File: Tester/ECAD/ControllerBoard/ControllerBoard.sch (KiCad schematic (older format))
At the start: 0 parts

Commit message: Progressed motor control PCB.
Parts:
- added J? (x4): Conn_01x02_Male, symbol Connector:Conn_01x02_Male
- added J?: Barrel_Jack, symbol Connector:Barrel_Jack
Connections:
- net labels added: +12V, GND
- wire segments 0 -> 24
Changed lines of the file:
@@
 $EndDescr
 $Sheet
-S 5100 1000 1450 5650
+S 5950 1250 2050 4650
 U 5E5070AC
 F0 "MCU" 50
 F1 "MCU.sch" 50
+F2 "MOTOR_CTRL_1A" O R 8000 1550 50
+F3 "MOTOR_CTRL_1B" O R 8000 1650 50
+F4 "MOTOR_CTRL_2A" O R 8000 1800 50
+F5 "MOTOR_CTRL_2B" O R 8000 1900 50
+F6 "MOTOR_CTRL_3A" O R 8000 2050 50
+F7 "MOTOR_CTRL_3B" O R 8000 2150 50
+F8 "MOTOR_CTRL_4A" O R 8000 2300 50
+F9 "MOTOR_CTRL_4B" O R 8000 2400 50
+F10 "MOTOR_FAULT_12" I R 8000 2550 50
+F11 "MOTOR_FAULT_34" I R 8000 2650 50
+F12 "MOTOR_SLEEP_12" O R 8000 2800 50
+F13 "MOTOR_SLEPP_34" O R 8000 2900 50
 $EndSheet
 $Sheet
-S 7200 1050 1200 950
+S 8650 1250 1350 2100
 U 5E507163
 F0 "Motor Control" 50
 F1 "MotorControl.sch" 50
+F2 "12V_POWER_IN" I L 8650 1350 50
+F3 "GND" I L 8650 3250 50
+F4 "MOTOR_OUT_2-" O R 10000 1700 50
+F5 "MOTOR_OUT_2+" O R 10000 1600 50
+F6 "MOTOR_OUT_1-" O R 10000 1450 50
+F7 "MOTOR_OUT_1+" O R 10000 1350 50
+F8 "MOTOR_OUT_4-" O R 10000 2200 50
+F9 "MOTOR_OUT_4+" O R 10000 2100 50
+F10 "MOTOR_OUT_3-" O R 10000 1950 50
+F11 "MOTOR_OUT_3+" O R 10000 1850 50
+F12 "MOTOR_CTRL_1A" I L 8650 1550 50
+F13 "MOTOR_CTRL_1B" I L 8650 1650 50
+F14 "MOTOR_CTRL_2A" I L 8650 1800 50
+F15 "MOTOR_CTRL_2B" I L 8650 1900 50
+F16 "MOTOR_CTRL_3A" I L 8650 2050 50
+F17 "MOTOR_CTRL_3B" I L 8650 2150 50
+F18 "MOTOR_CTRL_4A" I L 8650 2300 50
+F19 "MOTOR_CTRL_4B" I L 8650 2400 50
+F20 "MOTOR_FAULT_12" O L 8650 2550 50
+F21 "MOTOR_FAULT_34" O L 8650 2650 50
+F22 "MOTOR_SLEEP_12" I L 8650 2800 50
+F23 "MOTOR_SLEEP_34" I L 8650 2900 50
 $EndSheet
 $Sheet
-S 3000 1000 1400 5650
+S 3000 1250 1400 5650
 U 5E55806E
 F0 "Signal I/O" 50
 F1 "SignalInputOuput.sch" 50
 $EndSheet
+$Comp
+L Connector:Conn_01x02_Male J?
+U 1 1 5E51F506
+P 10200 1450
+AR Path="/5E507163/5E51F506" Ref="J?"  Part="1"
+AR Path="/5E51F506" Ref="J?"  Part="1"
+F 0 "J?" H 10172 1332 50  0000 R CNN
+F 1 "Conn_01x02_Male" H 10172 1423 50  0000 R CNN
+F 2 "" H 10200 1450 50  0001 C CNN
+F 3 "~" H 10200 1450 50  0001 C CNN
+	1    10200 1450
+	-1   0    0    1
+$EndComp
+$Comp
+L Connector:Conn_01x02_Male J?
+U 1 1 5E51F50C
+P 10200 1700
+AR Path="/5E507163/5E51F50C" Ref="J?"  Part="1"
+AR Path="/5E51F50C" Ref="J?"  Part="1"
+F 0 "J?" H 10172 1582 50  0000 R CNN
+F 1 "Conn_01x02_Male" H 10172 1673 50  0000 R CNN
+F 2 "" H 10200 1700 50  0001 C CNN
+F 3 "~" H 10200 1700 50  0001 C CNN
+	1    10200 1700
+	-1   0    0    1
+$EndComp
+$Comp
+L Connector:Conn_01x02_Male J?
+U 1 1 5E51F512
+P 10200 1950
+AR Path="/5E507163/5E51F512" Ref="J?"  Part="1"
+AR Path="/5E51F512" Ref="J?"  Part="1"
+F 0 "J?" H 10172 1832 50  0000 R CNN
+F 1 "Conn_01x02_Male" H 10172 1923 50  0000 R CNN
+F 2 "" H 10200 1950 50  0001 C CNN
+F 3 "~" H 10200 1950 50  0001 C CNN
+	1    10200 1950
+	-1   0    0    1
+$EndComp
+$Comp
+L Connector:Conn_01x02_Male J?
+U 1 1 5E51F518
+P 10200 2200
+AR Path="/5E507163/5E51F518" Ref="J?"  Part="1"
+AR Path="/5E51F518" Ref="J?"  Part="1"
+F 0 "J?" H 10172 2082 50  0000 R CNN
+F 1 "Conn_01x02_Male" H 10172 2173 50  0000 R CNN
+F 2 "" H 10200 2200 50  0001 C CNN
+F 3 "~" H 10200 2200 50  0001 C CNN
+	1    10200 2200
+	-1   0    0    1
+$EndComp
+$Comp
+L Connector:Barrel_Jack J?
+U 1 1 5E526230
+P 1050 1050
+F 0 "J?" H 1107 1375 50  0000 C CNN
+F 1 "Barrel_Jack" H 1107 1284 50  0000 C CNN
+F 2 "" H 1100 1010 50  0001 C CNN
+F 3 "~" H 1100 1010 50  0001 C CNN
+	1    1050 1050
+	1    0    0    -1
+$EndComp
+Wire Wire Line
+	1350 950  2050 950
+Wire Wire Line
+	6800 7550 4800 7550
+Wire Wire Line
+	1500 7550 1500 1150
+Wire Wire Line
+	1500 1150 1350 1150
+$Comp
+L power:GND #PWR?
+U 1 1 5E52861B
+P 4800 7550
+F 0 "#PWR?" H 4800 7300 50  0001 C CNN
+F 1 "GND" H 4805 7377 50  0000 C CNN
+F 2 "" H 4800 7550 50  0001 C CNN
+F 3 "" H 4800 7550 50  0001 C CNN
+	1    4800 7550
+	1    0    0    -1
+$EndComp
+Connection ~ 4800 7550
+Wire Wire Line
+	4800 7550 1500 7550
+$Comp
+L power:+12V #PWR?
+U 1 1 5E52879A
+P 2050 950
+F 0 "#PWR?" H 2050 800 50  0001 C CNN
+F 1 "+12V" H 2065 1123 50  0000 C CNN
+F 2 "" H 2050 950 50  0001 C CNN
+F 3 "" H 2050 950 50  0001 C CNN
+	1    2050 950
+	1    0    0    -1
+$EndComp
+Connection ~ 2050 950
+Wire Wire Line
+	6800 7550 6800 6300
+Wire Wire Line
+	8650 3250 8450 3250
+Wire Wire Line
+	8450 3250 8450 6300
+Wire Wire Line
+	6800 6300 8450 6300
+Wire Wire Line
+	8650 1350 8450 1350
+Wire Wire Line
+	8450 1350 8450 950
+Wire Wire Line
+	2050 950  8450 950
+Wire Wire Line
+	8000 1550 8650 1550
+Wire Wire Line
+	8650 1650 8000 1650
+Wire Wire Line
+	8000 1800 8650 1800
+Wire Wire Line
+	8650 1900 8000 1900
+Wire Wire Line
+	8000 2050 8650 2050
+Wire Wire Line
+	8650 2150 8000 2150
+Wire Wire Line
+	8000 2300 8650 2300
+Wire Wire Line
+	8650 2400 8000 2400
+Wire Wire Line
+	8000 2550 8650 2550
+Wire Wire Line
+	8650 2650 8000 2650
+Wire Wire Line
+	8000 2800 8650 2800
+Wire Wire Line
+	8650 2900 8000 2900
 $EndSCHEMATC

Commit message: Added the Manufacturer Part Number component field.
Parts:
- J? (x5): Manufacturer Part Number (none) -> tbd
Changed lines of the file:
@@
 F 2 "" H 10200 1450 50  0001 C CNN
 F 3 "~" H 10200 1450 50  0001 C CNN
+F 4 "tbd" H 10200 1450 50  0001 C CNN "Manufacturer Part Number"
 	1    10200 1450
 	-1   0    0    1
@@
 F 2 "" H 10200 1700 50  0001 C CNN
 F 3 "~" H 10200 1700 50  0001 C CNN
+F 4 "tbd" H 10200 1700 50  0001 C CNN "Manufacturer Part Number"
 	1    10200 1700
 	-1   0    0    1
@@
 F 2 "" H 10200 1950 50  0001 C CNN
 F 3 "~" H 10200 1950 50  0001 C CNN
+F 4 "tbd" H 10200 1950 50  0001 C CNN "Manufacturer Part Number"
 	1    10200 1950
 	-1   0    0    1
@@
 F 2 "" H 10200 2200 50  0001 C CNN
 F 3 "~" H 10200 2200 50  0001 C CNN
+F 4 "tbd" H 10200 2200 50  0001 C CNN "Manufacturer Part Number"
 	1    10200 2200
 	-1   0    0    1
@@
 F 2 "" H 1100 1010 50  0001 C CNN
 F 3 "~" H 1100 1010 50  0001 C CNN
+F 4 "tbd" H 1050 1050 50  0001 C CNN "Manufacturer Part Number"
 	1    1050 1050
 	1    0    0    -1

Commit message: Progressed component assignment.
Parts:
- J?: Manufacturer Part Number tbd -> PJ-037B
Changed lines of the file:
@@
 F 1 "Barrel_Jack" H 1107 1284 50  0000 C CNN
 F 2 "" H 1100 1010 50  0001 C CNN
-F 3 "~" H 1100 1010 50  0001 C CNN
-F 4 "tbd" H 1050 1050 50  0001 C CNN "Manufacturer Part Number"
+F 3 "https://www.cuidevices.com/product/resource/pj-037b.pdf" H 1100 1010 50  0001 C CNN
+F 4 "PJ-037B" H 1050 1050 50  0001 C CNN "Manufacturer Part Number"
 	1    1050 1050
 	1    0    0    -1

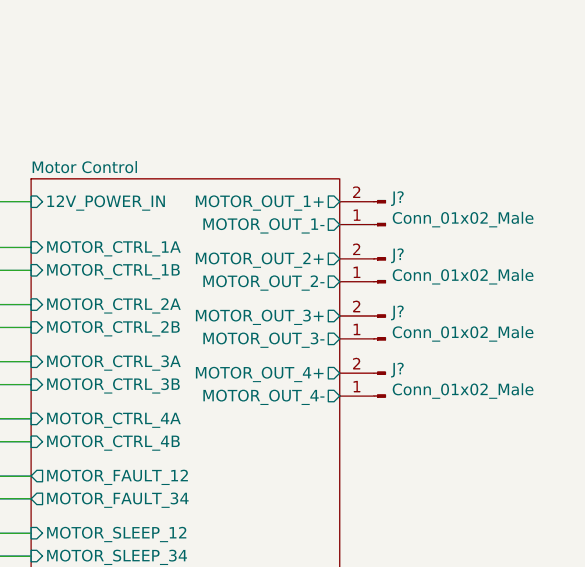
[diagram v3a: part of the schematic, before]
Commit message: Progressed component assigment.
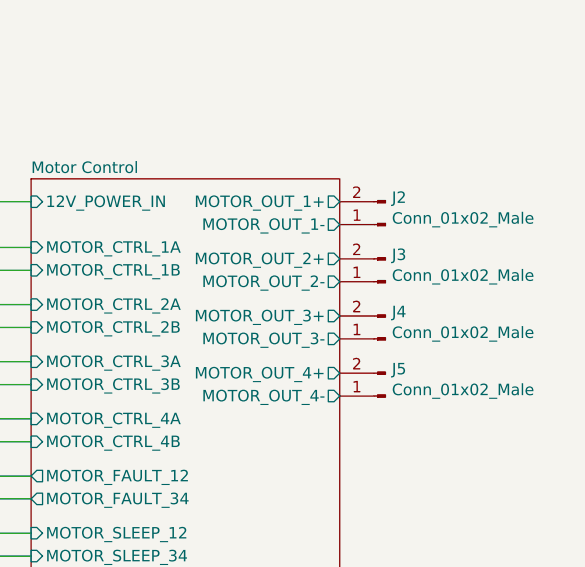
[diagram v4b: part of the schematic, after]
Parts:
- J2, J3, J4, J5: renamed from J?; Manufacturer Part Number tbd -> 0530480210
- gave numbers to parts that had none: 1
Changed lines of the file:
@@
 P 10200 1450
 AR Path="/5E507163/5E51F506" Ref="J?"  Part="1"
-AR Path="/5E51F506" Ref="J?"  Part="1"
-F 0 "J?" H 10172 1332 50  0000 R CNN
+AR Path="/5E51F506" Ref="J2"  Part="1"
+F 0 "J2" H 10172 1332 50  0000 R CNN
 F 1 "Conn_01x02_Male" H 10172 1423 50  0000 R CNN
 F 2 "" H 10200 1450 50  0001 C CNN
 F 3 "~" H 10200 1450 50  0001 C CNN
-F 4 "tbd" H 10200 1450 50  0001 C CNN "Manufacturer Part Number"
+F 4 "0530480210" H 10200 1450 50  0001 C CNN "Manufacturer Part Number"
 	1    10200 1450
 	-1   0    0    1
@@
 P 10200 1700
 AR Path="/5E507163/5E51F50C" Ref="J?"  Part="1"
-AR Path="/5E51F50C" Ref="J?"  Part="1"
-F 0 "J?" H 10172 1582 50  0000 R CNN
+AR Path="/5E51F50C" Ref="J3"  Part="1"
+F 0 "J3" H 10172 1582 50  0000 R CNN
 F 1 "Conn_01x02_Male" H 10172 1673 50  0000 R CNN
 F 2 "" H 10200 1700 50  0001 C CNN
 F 3 "~" H 10200 1700 50  0001 C CNN
-F 4 "tbd" H 10200 1700 50  0001 C CNN "Manufacturer Part Number"
+F 4 "0530480210" H 10200 1700 50  0001 C CNN "Manufacturer Part Number"
 	1    10200 1700
 	-1   0    0    1
@@
 P 10200 1950
 AR Path="/5E507163/5E51F512" Ref="J?"  Part="1"
-AR Path="/5E51F512" Ref="J?"  Part="1"
-F 0 "J?" H 10172 1832 50  0000 R CNN
+AR Path="/5E51F512" Ref="J4"  Part="1"
+F 0 "J4" H 10172 1832 50  0000 R CNN
 F 1 "Conn_01x02_Male" H 10172 1923 50  0000 R CNN
 F 2 "" H 10200 1950 50  0001 C CNN
 F 3 "~" H 10200 1950 50  0001 C CNN
-F 4 "tbd" H 10200 1950 50  0001 C CNN "Manufacturer Part Number"
+F 4 "0530480210" H 10200 1950 50  0001 C CNN "Manufacturer Part Number"
 	1    10200 1950
 	-1   0    0    1
@@
 P 10200 2200
 AR Path="/5E507163/5E51F518" Ref="J?"  Part="1"
-AR Path="/5E51F518" Ref="J?"  Part="1"
-F 0 "J?" H 10172 2082 50  0000 R CNN
+AR Path="/5E51F518" Ref="J5"  Part="1"
+F 0 "J5" H 10172 2082 50  0000 R CNN
 F 1 "Conn_01x02_Male" H 10172 2173 50  0000 R CNN
 F 2 "" H 10200 2200 50  0001 C CNN
 F 3 "~" H 10200 2200 50  0001 C CNN
-F 4 "tbd" H 10200 2200 50  0001 C CNN "Manufacturer Part Number"
+F 4 "0530480210" H 10200 2200 50  0001 C CNN "Manufacturer Part Number"
 	1    10200 2200
 	-1   0    0    1
 $EndComp
 $Comp
-L Connector:Barrel_Jack J?
+L Connector:Barrel_Jack J1
 U 1 1 5E526230
 P 1050 1050
-F 0 "J?" H 1107 1375 50  0000 C CNN
+F 0 "J1" H 1107 1375 50  0000 C CNN
 F 1 "Barrel_Jack" H 1107 1284 50  0000 C CNN
 F 2 "" H 1100 1010 50  0001 C CNN
@@
 	1500 1150 1350 1150
 $Comp
-L power:GND #PWR?
+L power:GND #PWR02
 U 1 1 5E52861B
 P 4800 7550
-F 0 "#PWR?" H 4800 7300 50  0001 C CNN
+F 0 "#PWR02" H 4800 7300 50  0001 C CNN
 F 1 "GND" H 4805 7377 50  0000 C CNN
 F 2 "" H 4800 7550 50  0001 C CNN
@@
 	4800 7550 1500 7550
 $Comp
-L power:+12V #PWR?
+L power:+12V #PWR01
 U 1 1 5E52879A
 P 2050 950
-F 0 "#PWR?" H 2050 800 50  0001 C CNN
+F 0 "#PWR01" H 2050 800 50  0001 C CNN
 F 1 "+12V" H 2065 1123 50  0000 C CNN
 F 2 "" H 2050 950 50  0001 C CNN

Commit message: Component assigment cont.
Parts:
- J2, J3, J4, J5: footprint (none) -> Connector_Molex:Molex_PicoBlade_53048-0210_1x02_P1.25mm_Horizontal
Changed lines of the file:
@@
 F 0 "J2" H 10172 1332 50  0000 R CNN
 F 1 "Conn_01x02_Male" H 10172 1423 50  0000 R CNN
-F 2 "" H 10200 1450 50  0001 C CNN
+F 2 "Connector_Molex:Molex_PicoBlade_53048-0210_1x02_P1.25mm_Horizontal" H 10200 1450 50  0001 C CNN
 F 3 "~" H 10200 1450 50  0001 C CNN
 F 4 "0530480210" H 10200 1450 50  0001 C CNN "Manufacturer Part Number"
@@
 F 0 "J3" H 10172 1582 50  0000 R CNN
 F 1 "Conn_01x02_Male" H 10172 1673 50  0000 R CNN
-F 2 "" H 10200 1700 50  0001 C CNN
+F 2 "Connector_Molex:Molex_PicoBlade_53048-0210_1x02_P1.25mm_Horizontal" H 10200 1700 50  0001 C CNN
 F 3 "~" H 10200 1700 50  0001 C CNN
 F 4 "0530480210" H 10200 1700 50  0001 C CNN "Manufacturer Part Number"
@@
 F 0 "J4" H 10172 1832 50  0000 R CNN
 F 1 "Conn_01x02_Male" H 10172 1923 50  0000 R CNN
-F 2 "" H 10200 1950 50  0001 C CNN
+F 2 "Connector_Molex:Molex_PicoBlade_53048-0210_1x02_P1.25mm_Horizontal" H 10200 1950 50  0001 C CNN
 F 3 "~" H 10200 1950 50  0001 C CNN
 F 4 "0530480210" H 10200 1950 50  0001 C CNN "Manufacturer Part Number"
@@
 F 0 "J5" H 10172 2082 50  0000 R CNN
 F 1 "Conn_01x02_Male" H 10172 2173 50  0000 R CNN
-F 2 "" H 10200 2200 50  0001 C CNN
+F 2 "Connector_Molex:Molex_PicoBlade_53048-0210_1x02_P1.25mm_Horizontal" H 10200 2200 50  0001 C CNN
 F 3 "~" H 10200 2200 50  0001 C CNN
 F 4 "0530480210" H 10200 2200 50  0001 C CNN "Manufacturer Part Number"

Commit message: Progressed control board schematic.
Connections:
- wire segments 24 -> 39
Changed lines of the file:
@@
 $Descr A4 11693 8268
 encoding utf-8
-Sheet 1 4
+Sheet 1 5
 Title ""
 Date ""
@@
 F11 "MOTOR_FAULT_34" I R 8000 2650 50
 F12 "MOTOR_SLEEP_12" O R 8000 2800 50
-F13 "MOTOR_SLEPP_34" O R 8000 2900 50
+F13 "MOTOR_SLEEP_34" O R 8000 2900 50
+F14 "GND" I L 5950 5800 50
+F15 "VMCU" I L 5950 1400 50
 $EndSheet
 $Sheet
@@
 F0 "Motor Control" 50
 F1 "MotorControl.sch" 50
-F2 "12V_POWER_IN" I L 8650 1350 50
-F3 "GND" I L 8650 3250 50
-F4 "MOTOR_OUT_2-" O R 10000 1700 50
-F5 "MOTOR_OUT_2+" O R 10000 1600 50
-F6 "MOTOR_OUT_1-" O R 10000 1450 50
-F7 "MOTOR_OUT_1+" O R 10000 1350 50
-F8 "MOTOR_OUT_4-" O R 10000 2200 50
-F9 "MOTOR_OUT_4+" O R 10000 2100 50
-F10 "MOTOR_OUT_3-" O R 10000 1950 50
-F11 "MOTOR_OUT_3+" O R 10000 1850 50
-F12 "MOTOR_CTRL_1A" I L 8650 1550 50
-F13 "MOTOR_CTRL_1B" I L 8650 1650 50
-F14 "MOTOR_CTRL_2A" I L 8650 1800 50
-F15 "MOTOR_CTRL_2B" I L 8650 1900 50
-F16 "MOTOR_CTRL_3A" I L 8650 2050 50
-F17 "MOTOR_CTRL_3B" I L 8650 2150 50
-F18 "MOTOR_CTRL_4A" I L 8650 2300 50
-F19 "MOTOR_CTRL_4B" I L 8650 2400 50
-F20 "MOTOR_FAULT_12" O L 8650 2550 50
-F21 "MOTOR_FAULT_34" O L 8650 2650 50
-F22 "MOTOR_SLEEP_12" I L 8650 2800 50
-F23 "MOTOR_SLEEP_34" I L 8650 2900 50
-$EndSheet
-$Sheet
-S 3000 1250 1400 5650
+F2 "GND" I L 8650 3250 50
+F3 "MOTOR_OUT_2-" O R 10000 1700 50
+F4 "MOTOR_OUT_2+" O R 10000 1600 50
+F5 "MOTOR_OUT_1-" O R 10000 1450 50
+F6 "MOTOR_OUT_1+" O R 10000 1350 50
+F7 "MOTOR_OUT_4-" O R 10000 2200 50
+F8 "MOTOR_OUT_4+" O R 10000 2100 50
+F9 "MOTOR_OUT_3-" O R 10000 1950 50
+F10 "MOTOR_OUT_3+" O R 10000 1850 50
+F11 "MOTOR_CTRL_1A" I L 8650 1550 50
+F12 "MOTOR_CTRL_1B" I L 8650 1650 50
+F13 "MOTOR_CTRL_2A" I L 8650 1800 50
+F14 "MOTOR_CTRL_2B" I L 8650 1900 50
+F15 "MOTOR_CTRL_3A" I L 8650 2050 50
+F16 "MOTOR_CTRL_3B" I L 8650 2150 50
+F17 "MOTOR_CTRL_4A" I L 8650 2300 50
+F18 "MOTOR_CTRL_4B" I L 8650 2400 50
+F19 "MOTOR_FAULT_12" O L 8650 2550 50
+F20 "MOTOR_FAULT_34" O L 8650 2650 50
+F21 "MOTOR_SLEEP_12" I L 8650 2800 50
+F22 "MOTOR_SLEEP_34" I L 8650 2900 50
+F23 "VMOTOR" I L 8650 1350 50
+$EndSheet
+$Sheet
+S 4100 1250 1400 5650
 U 5E55806E
 F0 "Signal I/O" 50
@@
 $EndComp
 Wire Wire Line
-	1350 950  2050 950
-Wire Wire Line
-	6800 7550 4800 7550
-Wire Wire Line
-	1500 7550 1500 1150
+	6800 7550 5750 7550
 Wire Wire Line
 	1500 1150 1350 1150
@@
 L power:+12V #PWR01
 U 1 1 5E52879A
-P 2050 950
-F 0 "#PWR01" H 2050 800 50  0001 C CNN
-F 1 "+12V" H 2065 1123 50  0000 C CNN
-F 2 "" H 2050 950 50  0001 C CNN
-F 3 "" H 2050 950 50  0001 C CNN
-	1    2050 950
+P 1550 950
+F 0 "#PWR01" H 1550 800 50  0001 C CNN
+F 1 "+12V" H 1565 1123 50  0000 C CNN
+F 2 "" H 1550 950 50  0001 C CNN
+F 3 "" H 1550 950 50  0001 C CNN
+	1    1550 950
 	1    0    0    -1
 $EndComp
-Connection ~ 2050 950
 Wire Wire Line
 	6800 7550 6800 6300
@@
 	6800 6300 8450 6300
 Wire Wire Line
-	8650 1350 8450 1350
-Wire Wire Line
-	8450 1350 8450 950
-Wire Wire Line
-	2050 950  8450 950
-Wire Wire Line
 	8000 1550 8650 1550
 Wire Wire Line
@@
 Wire Wire Line
 	8650 2900 8000 2900
+Wire Wire Line
+	5950 5800 5750 5800
+Wire Wire Line
+	5750 5800 5750 7550
+Connection ~ 5750 7550
+Wire Wire Line
+	5750 7550 4800 7550
+$Sheet
+S 1900 1250 1550 1700
+U 5E55CCDC
+F0 "Power" 50
+F1 "Power.sch" 50
+F2 "12V_POWER_IN" I L 1900 1350 50
+F3 "GND" I L 1900 2850 50
+F4 "VMOTOR" O R 3450 1350 50
+F5 "VMCU" O R 3450 1500 50
+$EndSheet
+Wire Wire Line
+	1700 950  1550 950
+Connection ~ 1550 950
+Wire Wire Line
+	1550 950  1350 950
+Wire Wire Line
+	1500 1150 1500 2850
+Wire Wire Line
+	1900 1350 1700 1350
+Wire Wire Line
+	1700 1350 1700 950
+Wire Wire Line
+	1900 2850 1500 2850
+Connection ~ 1500 2850
+Wire Wire Line
+	1500 2850 1500 7550
+Wire Wire Line
+	3450 1350 3650 1350
+Wire Wire Line
+	3650 1350 3650 650
+Wire Wire Line
+	3650 650  8400 650
+Wire Wire Line
+	8400 650  8400 1350
+Wire Wire Line
+	8400 1350 8650 1350
+Wire Wire Line
+	3450 1500 3850 1500
+Wire Wire Line
+	3850 1500 3850 800
+Wire Wire Line
+	3850 800  5700 800
+Wire Wire Line
+	5950 1400 5700 1400
+Wire Wire Line
+	5700 1400 5700 800
 $EndSCHEMATC

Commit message: Progressed circuit layout.
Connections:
- wire segments 39 -> 59
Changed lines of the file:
@@
 $EndDescr
-$Sheet
-S 5950 1250 2050 4650
-U 5E5070AC
-F0 "MCU" 50
-F1 "MCU.sch" 50
-F2 "MOTOR_CTRL_1A" O R 8000 1550 50
-F3 "MOTOR_CTRL_1B" O R 8000 1650 50
-F4 "MOTOR_CTRL_2A" O R 8000 1800 50
-F5 "MOTOR_CTRL_2B" O R 8000 1900 50
-F6 "MOTOR_CTRL_3A" O R 8000 2050 50
-F7 "MOTOR_CTRL_3B" O R 8000 2150 50
-F8 "MOTOR_CTRL_4A" O R 8000 2300 50
-F9 "MOTOR_CTRL_4B" O R 8000 2400 50
-F10 "MOTOR_FAULT_12" I R 8000 2550 50
-F11 "MOTOR_FAULT_34" I R 8000 2650 50
-F12 "MOTOR_SLEEP_12" O R 8000 2800 50
-F13 "MOTOR_SLEEP_34" O R 8000 2900 50
-F14 "GND" I L 5950 5800 50
-F15 "VMCU" I L 5950 1400 50
-$EndSheet
 $Sheet
 S 8650 1250 1350 2100
@@
 F23 "VMOTOR" I L 8650 1350 50
 $EndSheet
-$Sheet
-S 4100 1250 1400 5650
-U 5E55806E
-F0 "Signal I/O" 50
-F1 "SignalInputOuput.sch" 50
-$EndSheet
 $Comp
 L Connector:Conn_01x02_Male J?
@@
 L power:GND #PWR02
 U 1 1 5E52861B
-P 4800 7550
-F 0 "#PWR02" H 4800 7300 50  0001 C CNN
-F 1 "GND" H 4805 7377 50  0000 C CNN
-F 2 "" H 4800 7550 50  0001 C CNN
-F 3 "" H 4800 7550 50  0001 C CNN
-	1    4800 7550
+P 4600 7550
+F 0 "#PWR02" H 4600 7300 50  0001 C CNN
+F 1 "GND" H 4605 7377 50  0000 C CNN
+F 2 "" H 4600 7550 50  0001 C CNN
+F 3 "" H 4600 7550 50  0001 C CNN
+	1    4600 7550
 	1    0    0    -1
 $EndComp
-Connection ~ 4800 7550
-Wire Wire Line
-	4800 7550 1500 7550
 $Comp
 L power:+12V #PWR01
@@
 Wire Wire Line
 	5750 5800 5750 7550
-Connection ~ 5750 7550
-Wire Wire Line
-	5750 7550 4800 7550
+Wire Wire Line
+	1700 950  1550 950
+Connection ~ 1550 950
+Wire Wire Line
+	1550 950  1350 950
+Wire Wire Line
+	1900 1350 1700 1350
+Wire Wire Line
+	1700 1350 1700 950
+Wire Wire Line
+	8400 650  8400 1350
+Wire Wire Line
+	8400 1350 8650 1350
+Wire Wire Line
+	5950 1400 5700 1400
+Wire Wire Line
+	5700 1400 5700 800
 $Sheet
-S 1900 1250 1550 1700
+S 1900 1250 1200 1000
 U 5E55CCDC
 F0 "Power" 50
 F1 "Power.sch" 50
 F2 "12V_POWER_IN" I L 1900 1350 50
-F3 "GND" I L 1900 2850 50
-F4 "VMOTOR" O R 3450 1350 50
-F5 "VMCU" O R 3450 1500 50
+F3 "GND" I L 1900 2000 50
+F4 "VMOTOR" O R 3100 1350 50
+F5 "VMCU" O R 3100 1500 50
+F6 "VPOS_SENS_5V" O R 3100 1650 50
+F7 "VLASER_5V" O R 3100 1800 50
 $EndSheet
 Wire Wire Line
-	1700 950  1550 950
-Connection ~ 1550 950
-Wire Wire Line
-	1550 950  1350 950
-Wire Wire Line
-	1500 1150 1500 2850
-Wire Wire Line
-	1900 1350 1700 1350
-Wire Wire Line
-	1700 1350 1700 950
-Wire Wire Line
-	1900 2850 1500 2850
-Connection ~ 1500 2850
-Wire Wire Line
-	1500 2850 1500 7550
-Wire Wire Line
-	3450 1350 3650 1350
-Wire Wire Line
-	3650 1350 3650 650
-Wire Wire Line
-	3650 650  8400 650
-Wire Wire Line
-	8400 650  8400 1350
-Wire Wire Line
-	8400 1350 8650 1350
-Wire Wire Line
-	3450 1500 3850 1500
-Wire Wire Line
-	3850 1500 3850 800
-Wire Wire Line
-	3850 800  5700 800
-Wire Wire Line
-	5950 1400 5700 1400
-Wire Wire Line
-	5700 1400 5700 800
+	1500 1150 1500 2000
+Wire Wire Line
+	1900 2000 1500 2000
+Connection ~ 1500 2000
+Wire Wire Line
+	1500 2000 1500 7550
+Wire Wire Line
+	3100 1350 3350 1350
+Wire Wire Line
+	3350 1350 3350 650
+Wire Wire Line
+	3350 650  8400 650
+Wire Wire Line
+	3500 800  3500 1500
+Wire Wire Line
+	3500 1500 3100 1500
+Wire Wire Line
+	3500 800  5700 800
+Wire Wire Line
+	1500 7550 3850 7550
+Connection ~ 4600 7550
+Connection ~ 5750 7550
+$Sheet
+S 5950 1250 2050 4650
+U 5E5070AC
+F0 "MCU" 50
+F1 "MCU.sch" 50
+F2 "MOTOR_CTRL_1A" O R 8000 1550 50
+F3 "MOTOR_CTRL_1B" O R 8000 1650 50
+F4 "MOTOR_CTRL_2A" O R 8000 1800 50
+F5 "MOTOR_CTRL_2B" O R 8000 1900 50
+F6 "MOTOR_CTRL_3A" O R 8000 2050 50
+F7 "MOTOR_CTRL_3B" O R 8000 2150 50
+F8 "MOTOR_CTRL_4A" O R 8000 2300 50
+F9 "MOTOR_CTRL_4B" O R 8000 2400 50
+F10 "MOTOR_FAULT_12" I R 8000 2550 50
+F11 "MOTOR_FAULT_34" I R 8000 2650 50
+F12 "MOTOR_SLEEP_12" O R 8000 2800 50
+F13 "MOTOR_SLEEP_34" O R 8000 2900 50
+F14 "GND" I L 5950 5800 50
+F15 "VMCU" I L 5950 1400 50
+F16 "POS_MISO" I L 5950 1700 50
+F17 "POS_MOSI" O L 5950 1800 50
+F18 "POS_SCLK" O L 5950 1900 50
+F19 "~POSX_NCS" O L 5950 2050 50
+F20 "~POSY_NCS" O L 5950 2150 50
+F21 "~POSZ_NCS" O L 5950 2250 50
+F22 "POSX_MOTION" I L 5950 2400 50
+F23 "POSY_MOTION" I L 5950 2500 50
+F24 "POSZ_MOTION" I L 5950 2600 50
+F25 "~POSX_NRESET" O L 5950 2750 50
+F26 "~POSY_NRESET" O L 5950 2850 50
+F27 "~POSZ_NRESET" O L 5950 2950 50
+F28 "END_STOP_X" I L 5950 3100 50
+F29 "END_STOP_Y" I L 5950 3200 50
+F30 "END_STOP_Z" I L 5950 3300 50
+$EndSheet
+Wire Wire Line
+	4600 7550 5750 7550
+Wire Wire Line
+	5550 1700 5950 1700
+Wire Wire Line
+	5550 1800 5950 1800
+Wire Wire Line
+	5950 1900 5550 1900
+Wire Wire Line
+	5550 2050 5950 2050
+Wire Wire Line
+	5950 2150 5550 2150
+Wire Wire Line
+	5950 3300 5550 3300
+Wire Wire Line
+	5550 3200 5950 3200
+Wire Wire Line
+	5950 3100 5550 3100
+Wire Wire Line
+	5550 2950 5950 2950
+Wire Wire Line
+	5950 2850 5550 2850
+Wire Wire Line
+	5550 2600 5950 2600
+Wire Wire Line
+	5950 2500 5550 2500
+Wire Wire Line
+	5550 2400 5950 2400
+Wire Wire Line
+	5950 2250 5550 2250
+Wire Wire Line
+	3100 1650 4100 1650
+Wire Wire Line
+	3100 1800 4100 1800
+Wire Wire Line
+	5950 2750 5550 2750
+Wire Wire Line
+	4100 3350 3850 3350
+Wire Wire Line
+	3850 3350 3850 7550
+Connection ~ 3850 7550
+Wire Wire Line
+	3850 7550 4600 7550
+$Sheet
+S 4100 1500 1450 2000
+U 5E55806E
+F0 "Signal I/O" 50
+F1 "SignalInputOuput.sch" 50
+F2 "V_LASER_5V" I L 4100 1800 50
+F3 "VPOS_SENS_5V" I L 4100 1650 50
+F4 "GND" I L 4100 3350 50
+F5 "POS_MISO" O R 5550 1700 50
+F6 "POS_MOSI" I R 5550 1800 50
+F7 "POS_SCLK" I R 5550 1900 50
+F8 "~POSX_NCS" I R 5550 2050 50
+F9 "~POSY_NCS" I R 5550 2150 50
+F10 "~POSZ_NCS" I R 5550 2250 50
+F11 "POSX_MOTION" O R 5550 2400 50
+F12 "POSY_MOTION" O R 5550 2500 50
+F13 "POSZ_MOTION" O R 5550 2600 50
+F14 "~POSX_NRESET" I R 5550 2750 50
+F15 "~POSY_NRESET" I R 5550 2850 50
+F16 "~POSZ_NRESET" I R 5550 2950 50
+F17 "END_STOP_X" O R 5550 3100 50
+F18 "END_STOP_Y" O R 5550 3200 50
+F19 "END_STOP_Z" O R 5550 3300 50
+$EndSheet
 $EndSCHEMATC
